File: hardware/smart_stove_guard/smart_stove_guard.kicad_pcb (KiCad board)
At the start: 2 copper layers, 4.5 x 12.5 mm, 29 parts, among them IC1 BS412, J1 12401948E412A, J2 AX-1203D-LF, J3 IO Expansion, U1 ESP32-C6-WROOM-1-N4, U2 MLX90614ESF-AAA-000-TU, U3 AMS1117-3.3

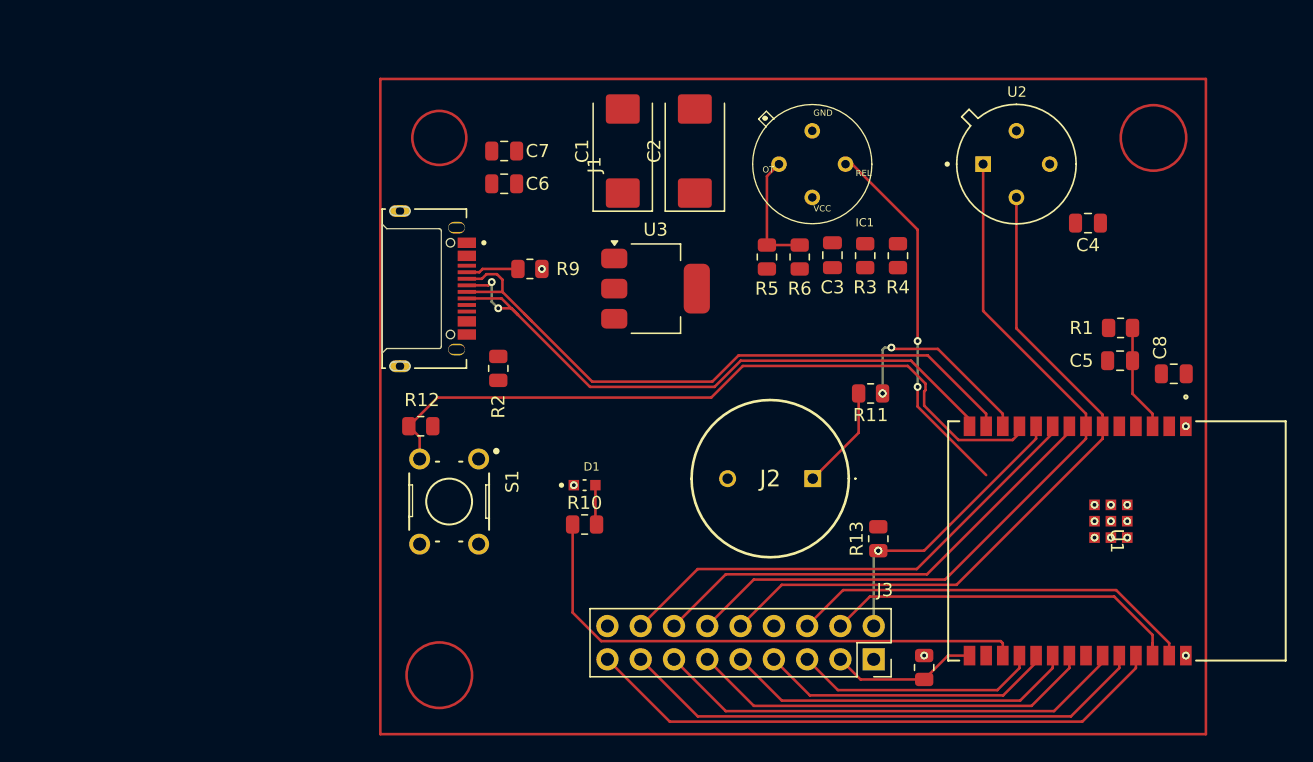
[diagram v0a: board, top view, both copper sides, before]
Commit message: ground pours and mounting
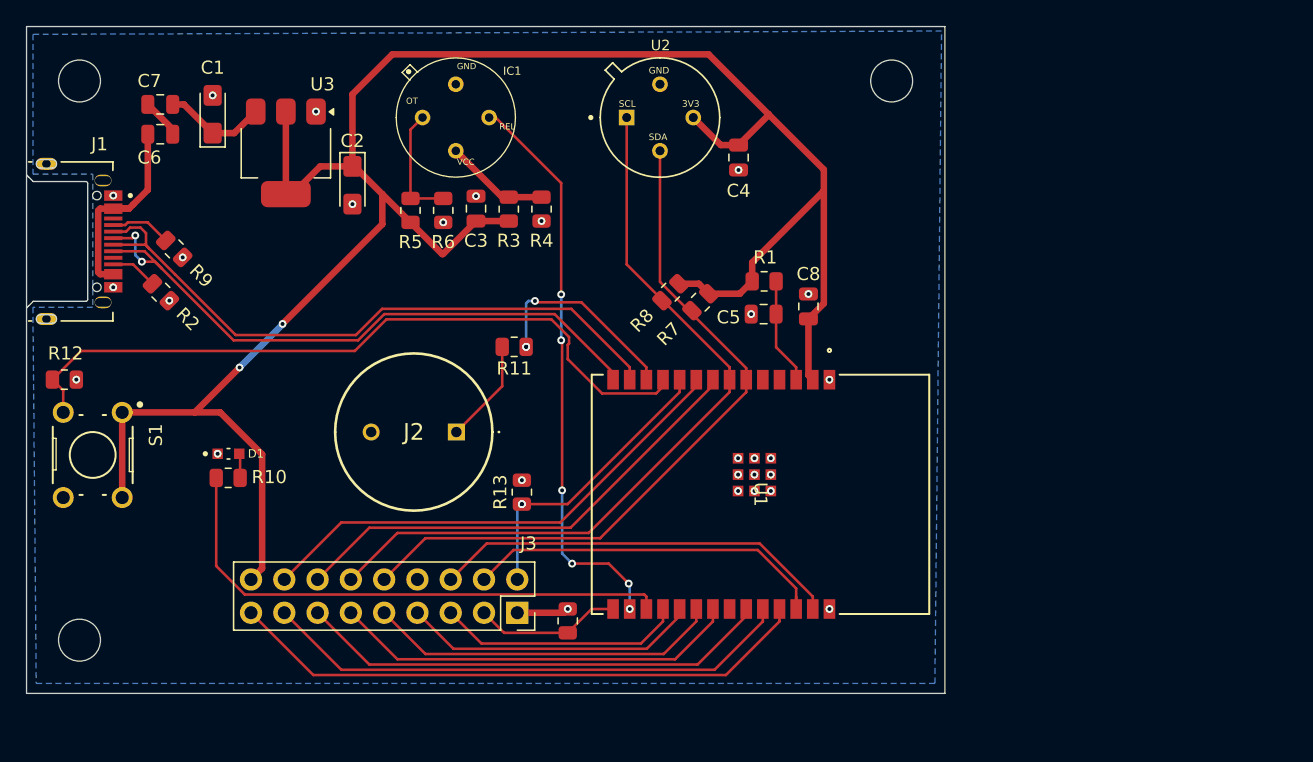
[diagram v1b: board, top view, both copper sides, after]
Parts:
- added R7: 4.7k, Resistor_SMD:R_0805_2012Metric, F.Cu at (129.4, 106.0)
- added R8: 4.7k, Resistor_SMD:R_0805_2012Metric, F.Cu at (127.1, 105.3)
- added REF**: MountingHole_3.2mm_M3, MountingHole:MountingHole_3.2mm_M3, F.Cu at (144.0, 89.2)
- added REF**: MountingHole_3.2mm_M3, MountingHole:MountingHole_3.2mm_M3, F.Cu at (82.0, 89.2)
- added REF**: MountingHole_3.2mm_M3, MountingHole:MountingHole_3.2mm_M3, F.Cu at (82.0, 131.8)
- C1, C2: footprint Capacitor_Tantalum_SMD:CP_EIA-7343-31_Kemet-D_HandSolder -> Capacitor_Tantalum_SMD:CP_EIA-3216-10_Kemet-I_HandSolder
- moved C1 31.4 mm to (92.2, 91.7)
- moved U3 30.1 mm to (97.8, 94.6), turned to -90 degrees
- moved C8 28.4 mm to (137.7, 106.4), turned to 90 degrees
- moved R1 27.4 mm to (134.3, 104.4)
- moved U1 27.4 mm to (134.0, 120.7)
- moved C3 27.4 mm to (112.3, 98.9)
- moved IC1 27.4 mm to (110.8, 89.4)
- moved J2 27.4 mm to (110.8, 115.9)
- moved J3 27.4 mm to (115.5, 129.7)
- moved R10 27.4 mm to (93.4, 119.4)
- moved R12 27.4 mm to (80.9, 111.9)
- moved R13 27.4 mm to (115.8, 120.5)
- moved R14 27.4 mm to (119.3, 130.4)
- moved R3 27.4 mm to (114.8, 98.9)
- moved R4 27.4 mm to (117.3, 98.9)
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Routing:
- net +3V3: track 0.00 -> 165.1 mm, vias 0 -> 2
- net Net-(C6-Pad2): track 0.00 -> 15.8 mm
- net MOTION: track 28.5 -> 43.9 mm, vias 2 -> 6
- net Net-(IC1-VDD): track 0.00 -> 8.00 mm
- net +5V: track 0.00 -> 7.92 mm
- net GND: track 0.00 -> 3.97 mm, vias 14 -> 28
- net Net-(J1-CC2): track 0.00 -> 3.60 mm
- net Net-(C6-Pad1): track 0.00 -> 3.06 mm
- net Net-(J1-CC1): track 4.01 -> 4.67 mm
- net D-: track 50.5 -> 49.9 mm
- net Net-(D1-PadA): track 3.04 -> 2.49 mm
- added copper zone on B.Cu, net GND
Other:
- board size 4.5 x 12.5 mm -> 70.1 x 50.9 mm
- board text added: "3V3"
- board text added: "GND"
- board text added: "SCL"
- board text added: "SDA"
